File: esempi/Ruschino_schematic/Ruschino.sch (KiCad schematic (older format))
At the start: 29 parts, among them IC1 L293D, J1 Arduino_Nano_Header, P1 OUT12, P10 SER, P11 EXT_MOT, P2 ALIM_HALL, P3 CONN_MOT1, P4 OUT34, P5 HALL_01, P6 HOLE1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

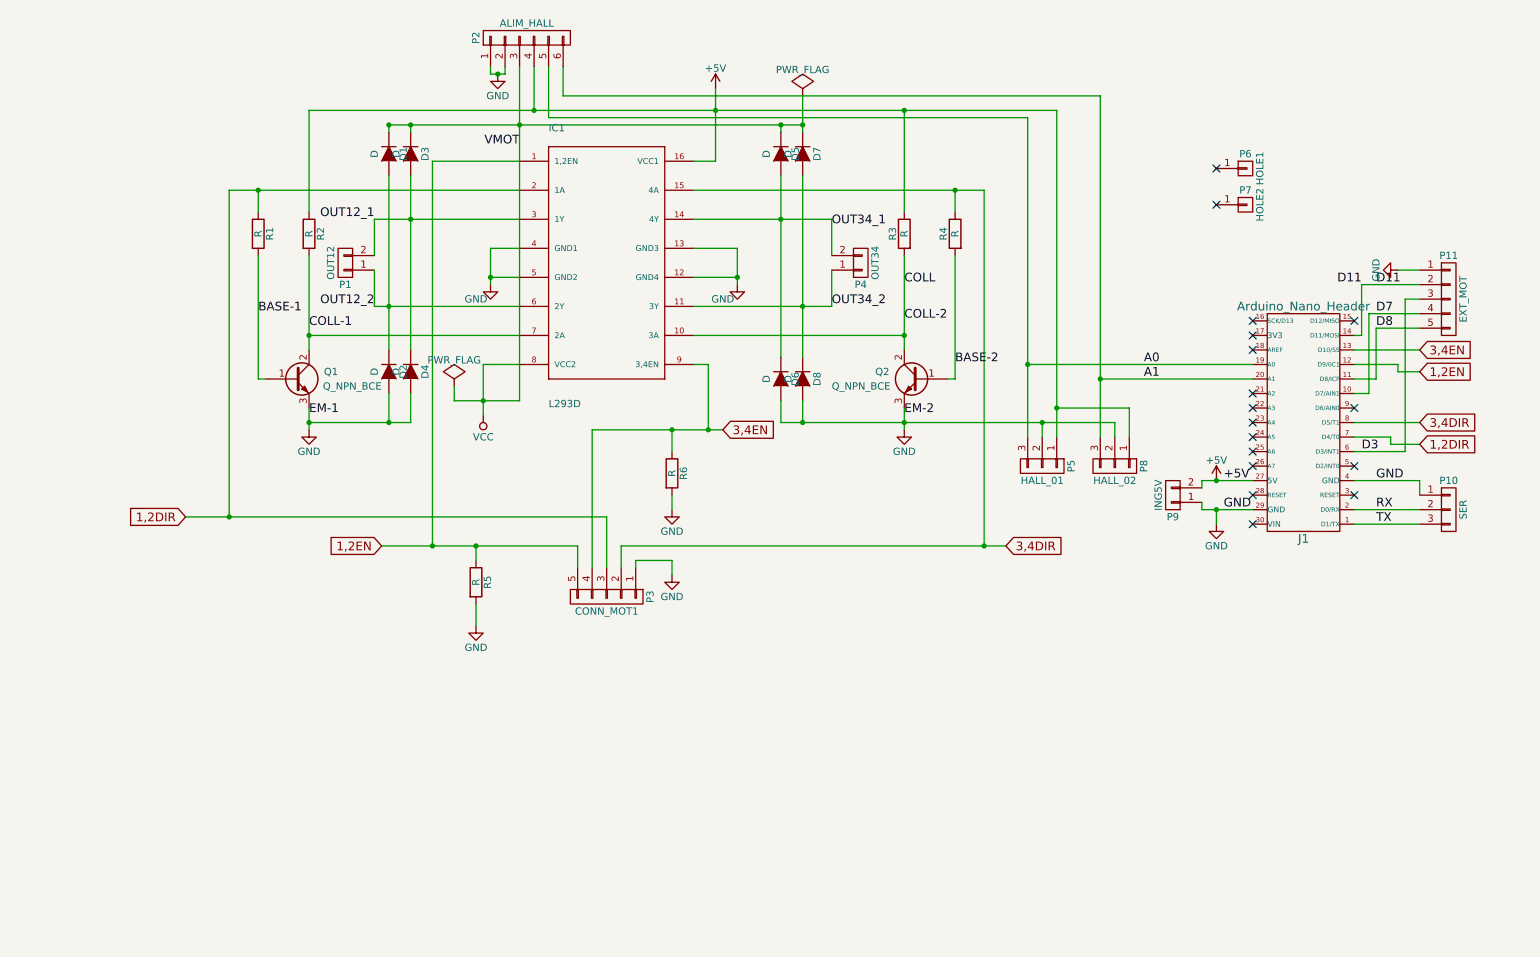
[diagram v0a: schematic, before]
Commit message: Modifiche a file ponte H eagginto adapter ESP012
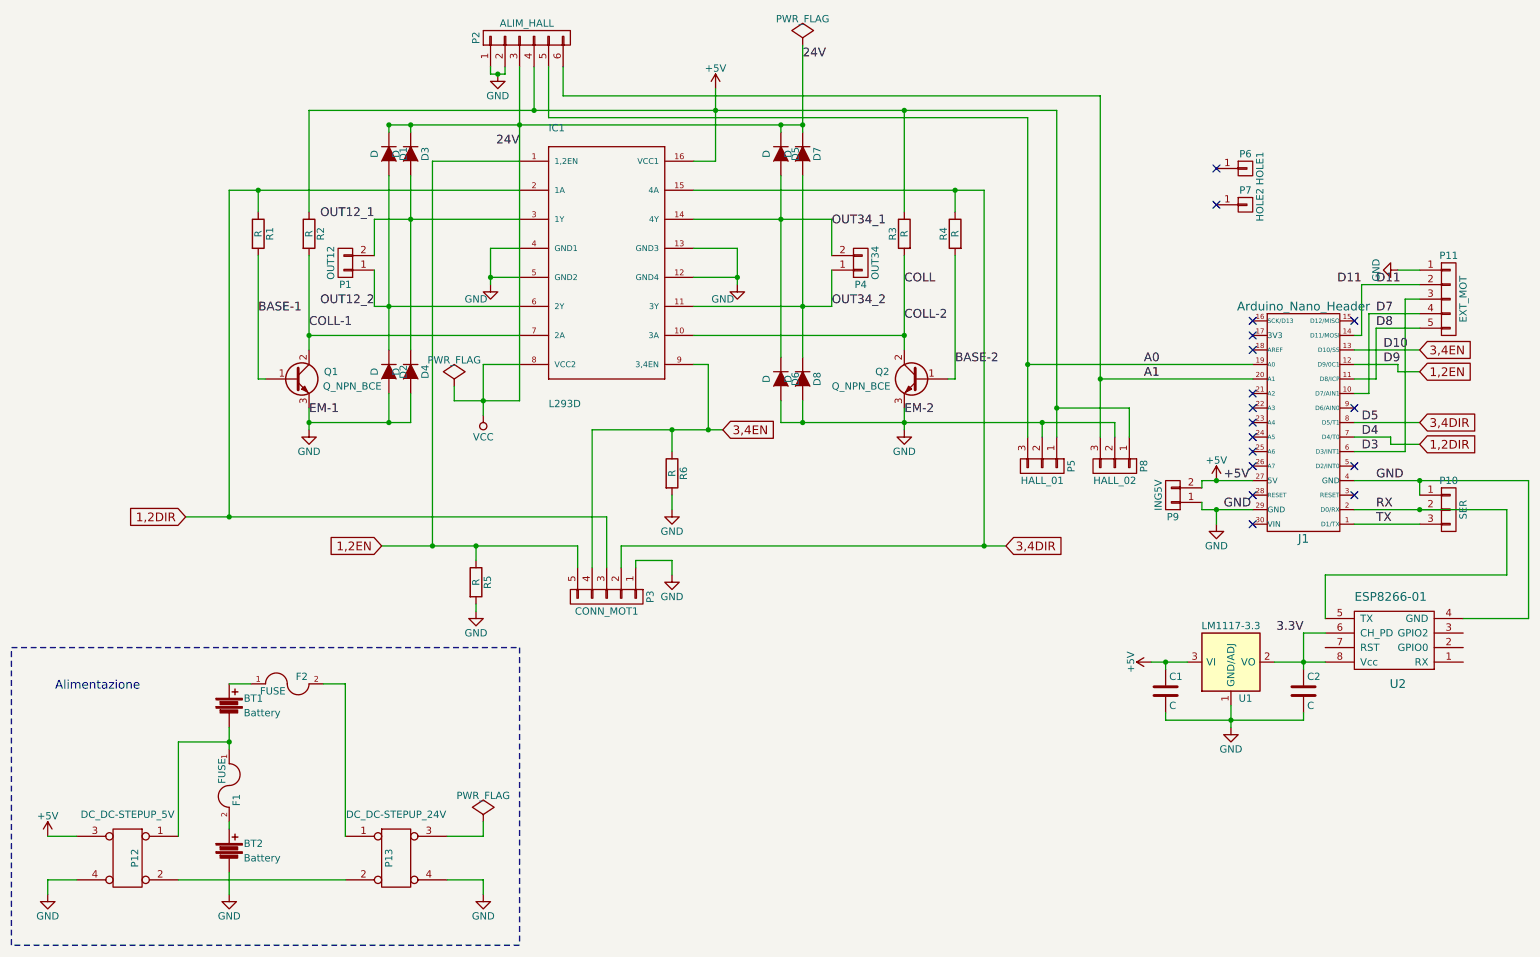
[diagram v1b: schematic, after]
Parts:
- added BT1, BT2: Battery, symbol Battery
- added C1, C2: C, symbol C
- added F1, F2: FUSE, symbol FUSE
- added P12: DC_DC-STEPUP_5V, symbol DC_DC
- added P13: DC_DC-STEPUP_24V, symbol DC_DC
- added U1: LM1117-3.3, symbol AP1117D33
- added U2: ESP8266-01, symbol ESP8266-01
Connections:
- net +5V: now also C1.1, P12.3 (P3), U1.3 (VI)
- net GND: now also BT2.2, C1.2, C2.2, P12.4 (P4), P13.4 (P4), U1.1 (GND/ADJ), U2.4 (GND)
- net RX: now also U2.5 (TX)
- new net: F2.2, P13.1 (P1)
- new net: P12.2 (P2), P13.2 (P2)
- new net: BT1.2, F1.1, P12.1 (P1)
- new net: BT2.1, F1.2
- new net: BT1.1, F2.1
- new net 3.3V: C2.1, U1.2 (VO), U2.6 (CH_PD), U2.8 (Vcc)
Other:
- note added: "Alimentazione"
